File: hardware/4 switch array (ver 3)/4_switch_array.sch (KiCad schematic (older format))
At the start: 17 parts, among them J1 Conn_01x04, J2 Conn_01x04, J3 Conn_01x02, J4 Conn_01x02, J5 Conn_01x02, J6 Conn_01x02, J7 Conn_01x02, Q1 Q_NPN_EBC, Q2 Q_NPN_EBC, Q3 Q_NPN_EBC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

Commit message: update v3 4 switch array
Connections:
- net +5V: now also J1.3 (Pin_3); no longer J1.1 (Pin_1)
- net GND: now also J1.4 (Pin_4), J2.4 (Pin_4); no longer J1.2 (Pin_2), J2.2 (Pin_2)
- net RCLK: now also J1.2 (Pin_2); no longer J1.4 (Pin_4)
- net SER_IN: now also J1.1 (Pin_1); no longer J1.3 (Pin_3)
- net SRCLK: now also J2.1 (Pin_1); no longer J2.3 (Pin_3)
- net SRCLR: now also J2.2 (Pin_2); no longer J2.4 (Pin_4)
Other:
- note added: "GND\n"
- note removed: "GND"
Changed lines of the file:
@@
 EESchema Schematic File Version 4
-LIBS:4_switch_array-cache
 EELAYER 30 0
 EELAYER END
@@
 	2850 3600 7750 3600
 Text Notes 8550 4850 2    100  ~ 0
-GND
+DATA 2
 Text Notes 8550 4650 2    100  ~ 0
+DATA 1
+Text Notes 8550 5050 2    100  ~ 0
 VCC
-Text Notes 8550 5050 2    100  ~ 0
-DATA 2
 Text Notes 8550 5250 2    100  ~ 0
-DATA 1
+GND\n
 Wire Notes Line style solid
 	8600 5300 7950 5300
@@
 	8600 4500 8600 5300
 Wire Notes Line style solid
+	8600 4850 9000 4850
+Wire Notes Line style solid
+	8600 4650 9000 4650
+Wire Notes Line style solid rgb(255, 0, 0)
+	8600 5050 9000 5050
+Wire Notes Line style solid rgb(0, 0, 0)
 	8600 5200 9000 5200
-Wire Notes Line style solid
-	8600 5000 9000 5000
-Wire Notes Line style solid rgb(255, 0, 0)
-	8600 4650 9000 4650
-Wire Notes Line style solid rgb(0, 0, 0)
-	8600 4800 9000 4800
 Text Notes 8750 4650 2    100  ~ 0
 1
@@
 Text GLabel 4350 2050 0    50   Input ~ 0
 SER_IN
-Text GLabel 3450 2250 2    50   Input ~ 0
+Text GLabel 3450 2050 2    50   Input ~ 0
 SER_IN
-Text GLabel 3450 2900 2    50   Input ~ 0
+Text GLabel 3450 2700 2    50   Input ~ 0
 SRCLR
 Wire Wire Line
 	4300 2650 4300 3150
-Text GLabel 3450 2350 2    50   Input ~ 0
+Text GLabel 3450 2150 2    50   Input ~ 0
 RCLK
 Text GLabel 4350 2550 0    50   Input ~ 0
@@
 Wire Wire Line
 	4500 2050 4350 2050
-$Comp
-L power:GND #PWR0112
-U 1 1 5E319499
-P 3600 2150
-F 0 "#PWR0112" H 3600 1900 50  0001 C CNN
-F 1 "GND" V 3600 1950 50  0000 C CNN
-F 2 "" H 3600 2150 50  0001 C CNN
-F 3 "" H 3600 2150 50  0001 C CNN
-	1    3600 2150
-	0    -1   -1   0
-$EndComp
 $Comp
 L Connector_Generic:Conn_01x04 J1
@@
 L power:GND #PWR0111
 U 1 1 5E32267D
-P 3600 2700
-F 0 "#PWR0111" H 3600 2450 50  0001 C CNN
-F 1 "GND" V 3600 2500 50  0000 C CNN
-F 2 "" H 3600 2700 50  0001 C CNN
-F 3 "" H 3600 2700 50  0001 C CNN
-	1    3600 2700
+P 3450 2900
+F 0 "#PWR0111" H 3450 2650 50  0001 C CNN
+F 1 "GND" V 3450 2700 50  0000 C CNN
+F 2 "" H 3450 2900 50  0001 C CNN
+F 3 "" H 3450 2900 50  0001 C CNN
+	1    3450 2900
 	0    -1   -1   0
 $EndComp
-Text GLabel 3450 2800 2    50   Input ~ 0
+Text GLabel 3450 2600 2    50   Input ~ 0
 SRCLK
-Wire Wire Line
-	3250 2150 3600 2150
-NoConn ~ 3250 2600
-Wire Wire Line
-	3250 2700 3600 2700
-Wire Wire Line
-	3250 2250 3450 2250
-Wire Wire Line
-	3250 2900 3450 2900
-Wire Wire Line
-	3250 2350 3450 2350
-Wire Wire Line
-	3250 2800 3450 2800
+NoConn ~ 3250 2800
+Wire Wire Line
+	3250 2900 3400 2900
 $Comp
 L power:+5V #PWR0103
 U 1 1 5F3567C2
-P 3650 2050
-F 0 "#PWR0103" H 3650 1900 50  0001 C CNN
-F 1 "+5V" H 3665 2223 50  0000 C CNN
-F 2 "" H 3650 2050 50  0001 C CNN
-F 3 "" H 3650 2050 50  0001 C CNN
-	1    3650 2050
-	1    0    0    -1
-$EndComp
-Wire Wire Line
-	3250 2050 3650 2050
+P 3600 2250
+F 0 "#PWR0103" H 3600 2100 50  0001 C CNN
+F 1 "+5V" H 3615 2423 50  0000 C CNN
+F 2 "" H 3600 2250 50  0001 C CNN
+F 3 "" H 3600 2250 50  0001 C CNN
+	1    3600 2250
+	0    1    1    0
+$EndComp
 Wire Wire Line
 	3250 4250 3600 4250
@@
 Wire Wire Line
 	5300 2750 5500 2750
+Wire Wire Line
+	3250 2050 3450 2050
+Wire Wire Line
+	3250 2150 3450 2150
+Wire Wire Line
+	3800 2350 3800 3000
+Wire Wire Line
+	3800 3000 3400 3000
+Wire Wire Line
+	3400 3000 3400 2900
+Wire Wire Line
+	3250 2350 3800 2350
+Connection ~ 3400 2900
+Wire Wire Line
+	3400 2900 3450 2900
+Wire Wire Line
+	3250 2250 3600 2250
+Wire Wire Line
+	3250 2600 3450 2600
+Wire Wire Line
+	3250 2700 3450 2700
 $EndSCHEMATC

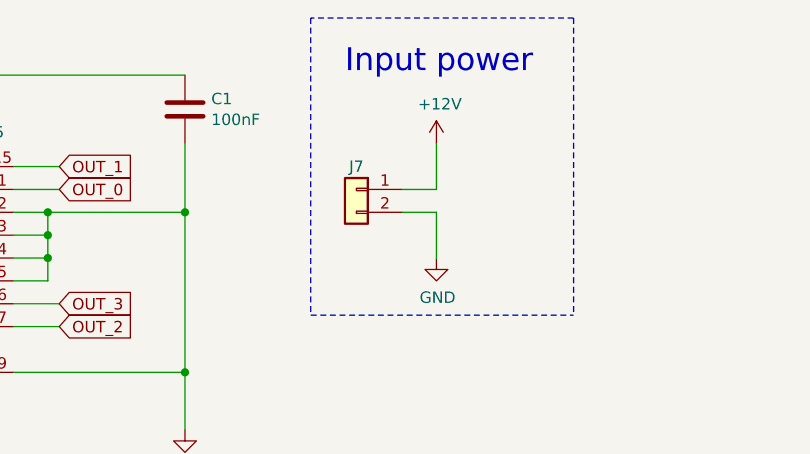
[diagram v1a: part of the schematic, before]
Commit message: Update on 12V5A system power line
- 12V5A power line is now represented by two connectors with 2 pins across all the modules
- all .png previews are updated. The central hub now has previews for schematics, PCB tracing and 3D model
- peltier module now has two 12V5A connectors with redesigned one side of the bridge. Now all MOSFETs can be equipped with heatsinks
- hum/temp sensor now has its connector position reversed to mimic Grove's one
- hum/temp and gas sensors now have a small BeeHive logo on front layer rather than one big on back layer
- hum/temp sensor now use only one layer for signals and one layer for ground
- switch arrays now have two connectors for 12V5A and 5V3A power lines
- switch arrays had their power lines better traced (no sharp turns)
- power supply (12V5A to 5V3A) now has two connectors for 12V5A power line
- one trace of power supply, which lies in between LM2596's legs, was narrowed to ensure that it will not be accidentally soldered or damaged during placement
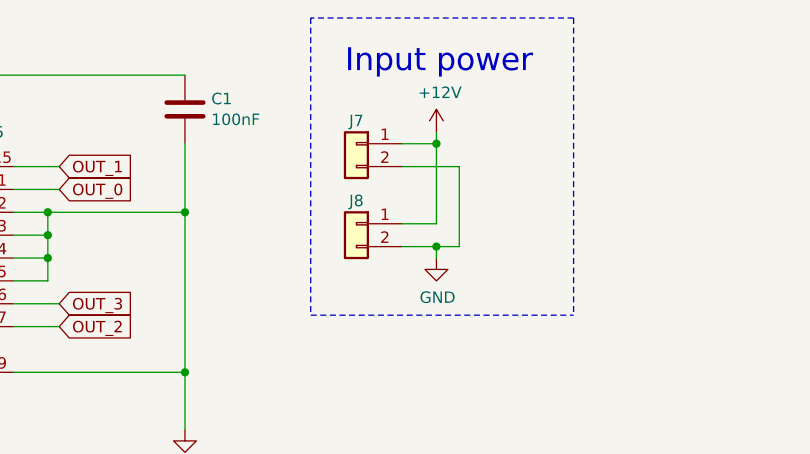
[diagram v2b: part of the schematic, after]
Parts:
- added J8: Conn_01x02, Connector_JST:JST_XH_B2B-XH-A_1x02_P2.50mm_Vertical, symbol Connector_Generic:Conn_01x02
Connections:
- net +12V: now also J8.1 (Pin_1)
- net GND: now also J8.2 (Pin_2)
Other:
- moved on the sheet: J7
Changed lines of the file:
@@
 L Connector_Generic:Conn_01x02 J7
 U 1 1 5E272691
-P 6800 2150
-F 0 "J7" H 6800 2250 50  0000 C CNN
-F 1 "Conn_01x02" H 6718 1916 50  0001 C CNN
-F 2 "Connector_JST:JST_XH_B2B-XH-A_1x02_P2.50mm_Vertical" H 6800 2150 50  0001 C CNN
-F 3 "~" H 6800 2150 50  0001 C CNN
-	1    6800 2150
+P 6800 1950
+F 0 "J7" H 6800 2050 50  0000 C CNN
+F 1 "Conn_01x02" H 6718 1716 50  0001 C CNN
+F 2 "Connector_JST:JST_XH_B2B-XH-A_1x02_P2.50mm_Vertical" H 6800 1950 50  0001 C CNN
+F 3 "~" H 6800 1950 50  0001 C CNN
+	1    6800 1950
 	-1   0    0    -1
 $EndComp
@@
 	1    0    0    -1
 $EndComp
-Wire Wire Line
-	7150 2250 7150 2450
-Wire Wire Line
-	7150 2150 7150 1950
 $Comp
 L Connector_Generic:Conn_01x02 J5
@@
 	1    0    0    -1
 $EndComp
-Wire Wire Line
-	7000 2250 7150 2250
-Wire Wire Line
-	7000 2150 7150 2150
 Text GLabel 4350 2050 0    50   Input ~ 0
 SER_IN
@@
 L power:+12V #PWR0104
 U 1 1 5F396714
-P 7150 1950
-F 0 "#PWR0104" H 7150 1800 50  0001 C CNN
-F 1 "+12V" H 7165 2123 50  0000 C CNN
-F 2 "" H 7150 1950 50  0001 C CNN
-F 3 "" H 7150 1950 50  0001 C CNN
-	1    7150 1950
+P 7150 1900
+F 0 "#PWR0104" H 7150 1750 50  0001 C CNN
+F 1 "+12V" H 7165 2073 50  0000 C CNN
+F 2 "" H 7150 1900 50  0001 C CNN
+F 3 "" H 7150 1900 50  0001 C CNN
+	1    7150 1900
 	1    0    0    -1
 $EndComp
@@
 Wire Wire Line
 	3250 2700 3450 2700
+$Comp
+L Connector_Generic:Conn_01x02 J8
+U 1 1 5FD25C64
+P 6800 2300
+F 0 "J8" H 6800 2400 50  0000 C CNN
+F 1 "Conn_01x02" H 6718 2066 50  0001 C CNN
+F 2 "Connector_JST:JST_XH_B2B-XH-A_1x02_P2.50mm_Vertical" H 6800 2300 50  0001 C CNN
+F 3 "~" H 6800 2300 50  0001 C CNN
+	1    6800 2300
+	-1   0    0    -1
+$EndComp
+Wire Wire Line
+	7000 1950 7150 1950
+Wire Wire Line
+	7150 1900 7150 1950
+Connection ~ 7150 1950
+Wire Wire Line
+	7000 2400 7150 2400
+Wire Wire Line
+	7150 2400 7150 2450
+Wire Wire Line
+	7000 2050 7250 2050
+Wire Wire Line
+	7250 2050 7250 2400
+Wire Wire Line
+	7250 2400 7150 2400
+Connection ~ 7150 2400
+Wire Wire Line
+	7150 2300 7000 2300
+Wire Wire Line
+	7150 1950 7150 2300
 $EndSCHEMATC
